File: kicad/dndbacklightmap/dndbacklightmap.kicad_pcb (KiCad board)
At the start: 2 copper layers, 76.2 x 76.2 mm, 40 parts, among them U1 SN65HVD230, U10 SLSS49E, U11 SLSS49E, U2 WeAct-STM32G431CoreBoard, U3 SLSS49E, U4 SLSS49E, U5 SLSS49E, U6 SLSS49E, U7 SLSS49E, U8 SLSS49E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

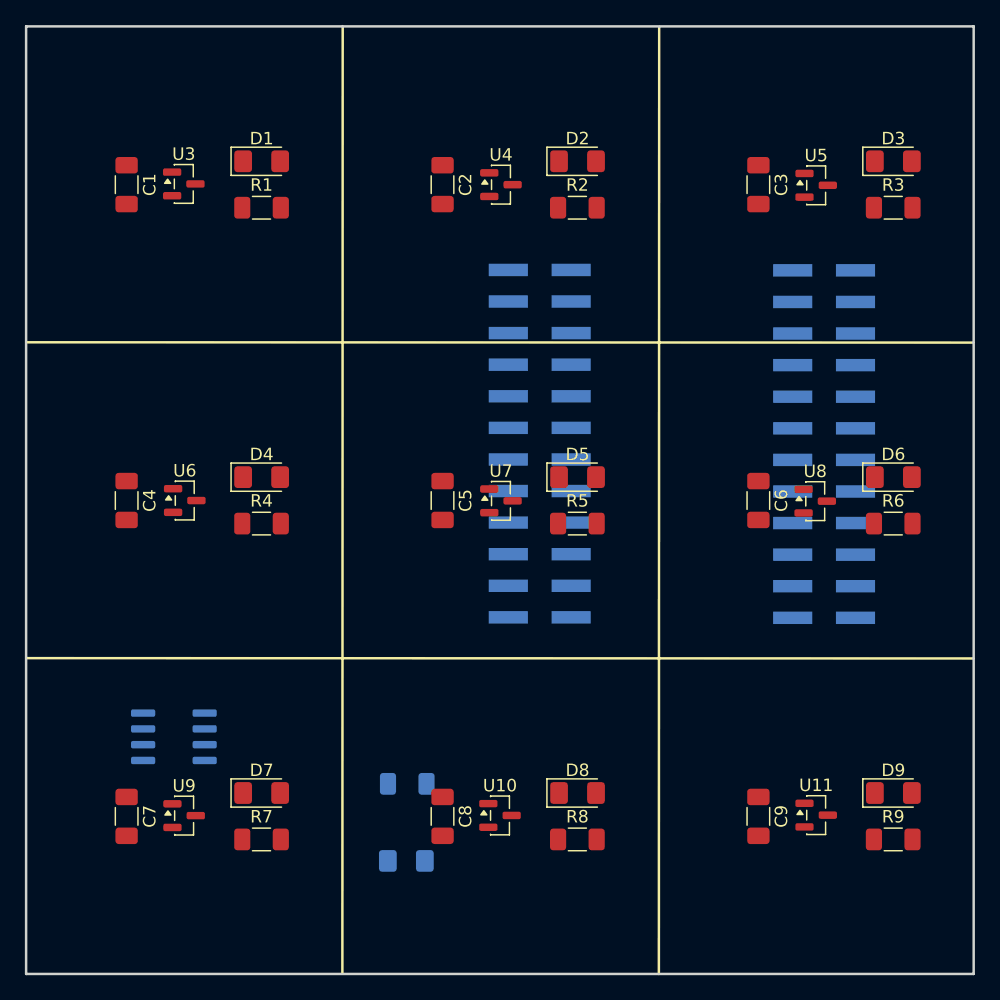
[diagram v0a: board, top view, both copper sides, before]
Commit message: rotation of components
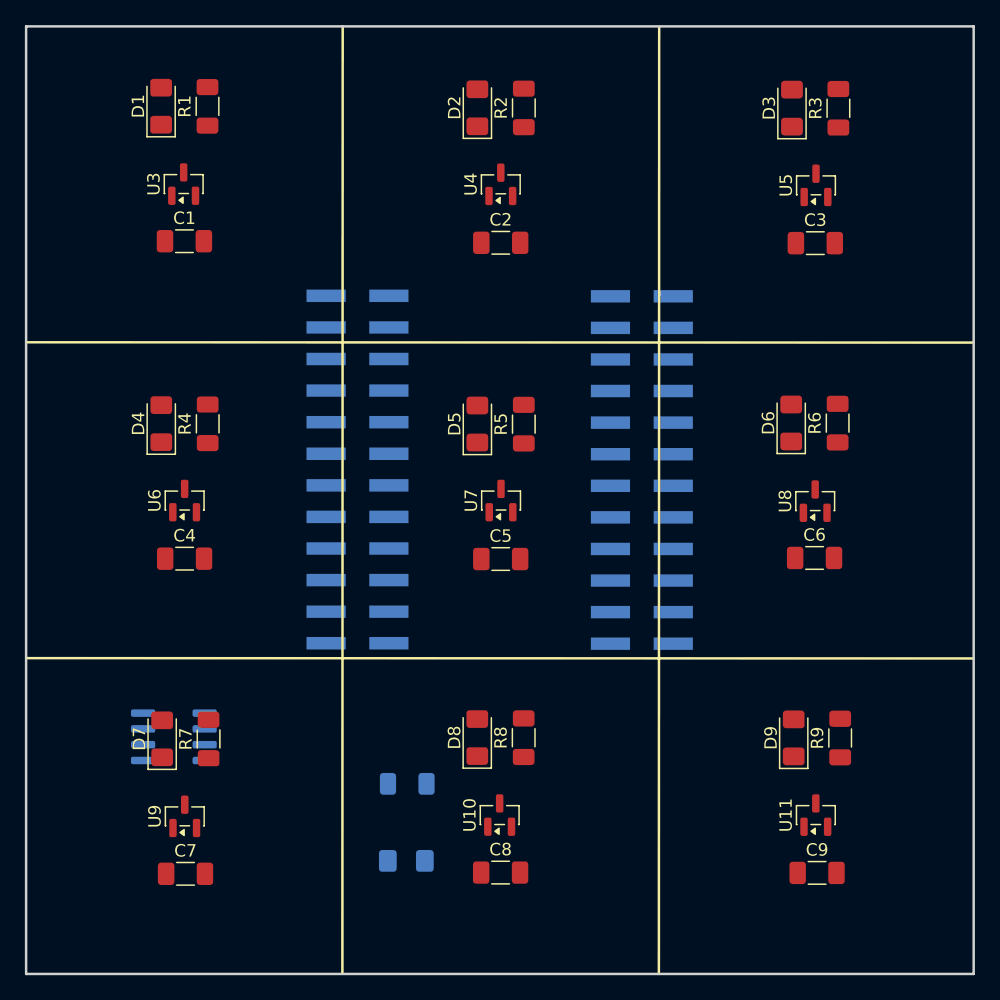
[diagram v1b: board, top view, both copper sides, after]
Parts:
- moved U2 14.8 mm to (146.0, 73.3)
- moved D6 9.30 mm to (155.3, 90.5), turned to 90 degrees
- moved R8 9.25 mm to (133.8, 115.8), turned to 90 degrees
- moved R1 9.24 mm to (108.4, 65.0), turned to 90 degrees
- moved R6 9.23 mm to (159.1, 90.5), turned to 90 degrees
- moved D1 9.22 mm to (104.6, 65.0), turned to 90 degrees
- moved D8 9.21 mm to (130.1, 115.8), turned to 90 degrees
- moved D3 9.21 mm to (155.4, 65.2), turned to 90 degrees
- moved R9 9.20 mm to (159.3, 115.8), turned to 90 degrees
- moved D9 9.16 mm to (155.5, 115.8), turned to 90 degrees
- moved D4 9.15 mm to (104.7, 90.5), turned to 90 degrees
- moved R7 9.13 mm to (108.5, 115.9), turned to 90 degrees
- moved R3 9.13 mm to (159.1, 65.2), turned to 90 degrees
- moved D2 9.13 mm to (130.1, 65.1), turned to 90 degrees
- moved R4 9.12 mm to (108.4, 90.6), turned to 90 degrees
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
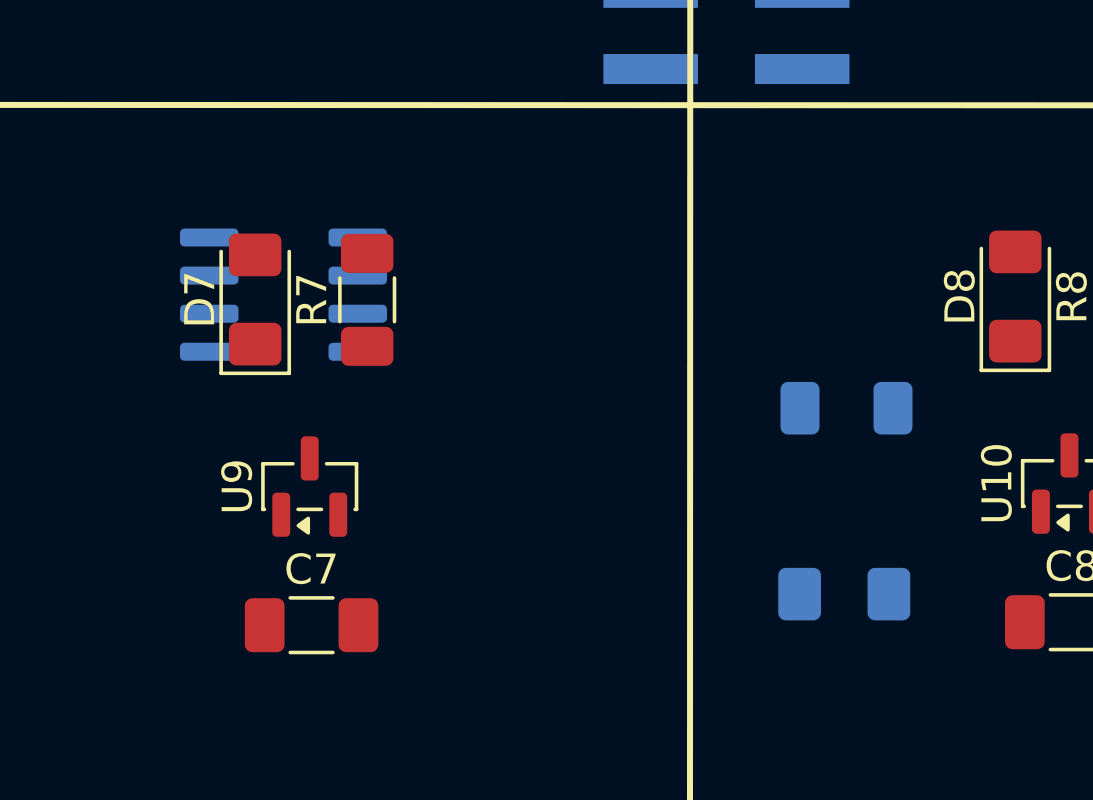
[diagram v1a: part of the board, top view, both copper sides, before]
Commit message: rotation of components
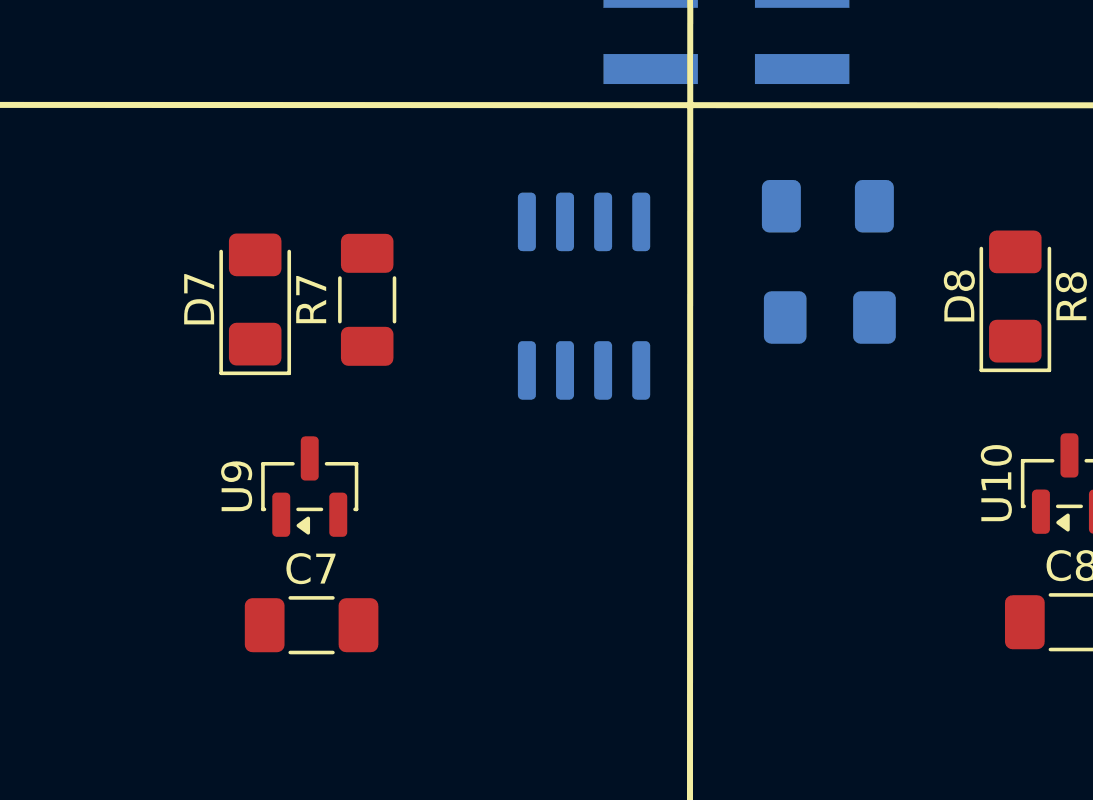
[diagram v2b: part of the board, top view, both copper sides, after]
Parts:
- moved U1 10.0 mm to (115.7, 115.8), turned to -90 degrees
- moved D10 9.23 mm to (123.9, 116.5)
- moved R10 6.76 mm to (123.8, 112.8)
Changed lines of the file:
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@@
 	(footprint "Resistor_SMD:R_1206_3216Metric_Pad1.30x1.75mm_HandSolder"
 		(layer "B.Cu")
-		(at 124.4451 119.507)
+		(at 123.8244 112.776)
 		(descr "Resistor SMD 1206 (3216 Metric), square (rectangular) end terminal, IPC-7351 nominal with elongated pad for handsoldering. (Body size source: IPC-SM-782 page 72, https://www.pcb-3d.com/wordpress/wp-content/uploads/ipc-sm-782a_amendment_1_and_2.pdf), generated with kicad-footprint-generator")
 		(tags "resistor handsolder")
@@
 	(footprint "Package_SO:SOIC-8_3.9x4.9mm_P1.27mm"
 		(layer "B.Cu")
-		(at 105.6782 115.7224)
+		(at 115.697 115.7732 -90)
 		(descr "SOIC, 8 Pin (JEDEC MS-012AA, https://www.analog.com/media/en/package-pcb-resources/package/pkg_pdf/soic_narrow-r/r_8.pdf), generated with kicad-footprint-generator ipc_gullwing_generator.py")
 		(tags "SOIC SO")
 		(property "Reference" "U1"
-			(at 0 3.4 180)
+			(at 0 3.4 90)
 			(layer "B.SilkS")
 			(effects
@@
 		)
 		(property "Value" "SN65HVD230"
-			(at 0 -3.4 180)
+			(at 0 -3.4 90)
 			(layer "B.Fab")
 			(effects
@@
 		)
 		(property "Datasheet" "http://www.ti.com/lit/ds/symlink/sn65hvd230.pdf"
-			(at 0 0 180)
+			(at 0 0 90)
 			(layer "B.Fab")
 			(hide yes)
@@
 		)
 		(property "Description" "CAN Bus Transceivers, 3.3V, 1Mbps, Low-Power capabilities, SOIC-8"
-			(at 0 0 180)
+			(at 0 0 90)
 			(layer "B.Fab")
 			(hide yes)
@@
 		(attr smd)
 		(fp_line
+			(start -2.06 2.56)
+			(end 2.06 2.56)
+			(stroke
+				(width 0.12)
+				(type solid)
+			)
+			(layer "B.SilkS")
+		)
+		(fp_line
+			(start 2.06 2.56)
+			(end 2.06 2.465)
+			(stroke
+				(width 0.12)
+				(type solid)
+			)
+			(layer "B.SilkS")
+		)
+		(fp_line
+			(start -2.06 2.465)
+			(end -2.06 2.56)
+			(stroke
+				(width 0.12)
+				(type solid)
+			)
+			(layer "B.SilkS")
+		)
+		(fp_line
+			(start 2.06 -2.465)
+			(end 2.06 -2.56)
+			(stroke
+				(width 0.12)
+				(type solid)
+			)
+			(layer "B.SilkS")
+		)
+		(fp_line
 			(start -2.06 -2.56)
 			(end -2.06 -2.465)
@@
 		)
 		(fp_line
-			(start -2.06 2.465)
-			(end -2.06 2.56)
-			(stroke
-				(width 0.12)
-				(type solid)
-			)
-			(layer "B.SilkS")
-		)
-		(fp_line
-			(start -2.06 2.56)
-			(end 2.06 2.56)
-			(stroke
-				(width 0.12)
-				(type solid)
-			)
-			(layer "B.SilkS")
-		)
-		(fp_line
 			(start 2.06 -2.56)
 			(end -2.06 -2.56)
-			(stroke
-				(width 0.12)
-				(type solid)
-			)
-			(layer "B.SilkS")
-		)
-		(fp_line
-			(start 2.06 -2.465)
-			(end 2.06 -2.56)
-			(stroke
-				(width 0.12)
-				(type solid)
-			)
-			(layer "B.SilkS")
-		)
-		(fp_line
-			(start 2.06 2.56)
-			(end 2.06 2.465)
 			(stroke
 				(width 0.12)
@@
 		)
 		(fp_line
+			(start -2.2 2.7)
+			(end 2.2 2.7)
+			(stroke
+				(width 0.05)
+				(type solid)
+			)
+			(layer "B.CrtYd")
+		)
+		(fp_line
+			(start 2.2 2.7)
+			(end 2.2 2.46)
+			(stroke
+				(width 0.05)
+				(type solid)
+			)
+			(layer "B.CrtYd")
+		)
+		(fp_line
+			(start -3.7 2.46)
+			(end -2.2 2.46)
+			(stroke
+				(width 0.05)
+				(type solid)
+			)
+			(layer "B.CrtYd")
+		)
+		(fp_line
+			(start -2.2 2.46)
+			(end -2.2 2.7)
+			(stroke
+				(width 0.05)
+				(type solid)
+			)
+			(layer "B.CrtYd")
+		)
+		(fp_line
+			(start 2.2 2.46)
+			(end 3.7 2.46)
+			(stroke
+				(width 0.05)
+				(type solid)
+			)
+			(layer "B.CrtYd")
+		)
+		(fp_line
+			(start 3.7 2.46)
+			(end 3.7 -2.46)
+			(stroke
+				(width 0.05)
+				(type solid)
+			)
+			(layer "B.CrtYd")
+		)
+		(fp_line
 			(start -3.7 -2.46)
 			(end -3.7 2.46)
@@
 		)
 		(fp_line
-			(start -3.7 2.46)
-			(end -2.2 2.46)
+			(start -2.2 -2.46)
+			(end -3.7 -2.46)
+			(stroke
+				(width 0.05)
+				(type solid)
+			)
+			(layer "B.CrtYd")
+		)
+		(fp_line
+			(start 2.2 -2.46)
+			(end 2.2 -2.7)
+			(stroke
+				(width 0.05)
+				(type solid)
+			)
+			(layer "B.CrtYd")
+		)
+		(fp_line
+			(start 3.7 -2.46)
+			(end 2.2 -2.46)
 			(stroke
 				(width 0.05)
@@
 		)
 		(fp_line
-			(start -2.2 -2.46)
-			(end -3.7 -2.46)
-			(stroke
-				(width 0.05)
-				(type solid)
-			)
-			(layer "B.CrtYd")
-		)
-		(fp_line
-			(start -2.2 2.46)
-			(end -2.2 2.7)
-			(stroke
-				(width 0.05)
-				(type solid)
-			)
-			(layer "B.CrtYd")
-		)
-		(fp_line
-			(start -2.2 2.7)
-			(end 2.2 2.7)
-			(stroke
-				(width 0.05)
-				(type solid)
-			)
-			(layer "B.CrtYd")
-		)
-		(fp_line
 			(start 2.2 -2.7)
 			(end -2.2 -2.7)
-			(stroke
-				(width 0.05)
-				(type solid)
-			)
-			(layer "B.CrtYd")
-		)
-		(fp_line
-			(start 2.2 -2.46)
-			(end 2.2 -2.7)
-			(stroke
-				(width 0.05)
-				(type solid)
-			)
-			(layer "B.CrtYd")
-		)
-		(fp_line
-			(start 2.2 2.46)
-			(end 3.7 2.46)
-			(stroke
-				(width 0.05)
-				(type solid)
-			)
-			(layer "B.CrtYd")
-		)
-		(fp_line
-			(start 2.2 2.7)
-			(end 2.2 2.46)
-			(stroke
-				(width 0.05)
-				(type solid)
-			)
-			(layer "B.CrtYd")
-		)
-		(fp_line
-			(start 3.7 -2.46)
-			(end 2.2 -2.46)
-			(stroke
-				(width 0.05)
-				(type solid)
-			)
-			(layer "B.CrtYd")
-		)
-		(fp_line
-			(start 3.7 2.46)
-			(end 3.7 -2.46)
 			(stroke
 				(width 0.05)
@@
 		)
 		(fp_text user "${REFERENCE}"
-			(at 0 0 90)
+			(at 0 0 0)
 			(layer "B.Fab")
 			(effects
@@
 		)
 		(pad "1" smd roundrect
-			(at -2.475 1.905)
+			(at -2.475 1.905 270)
 			(size 1.95 0.6)
 			(layers "B.Cu" "B.Mask" "B.Paste")
@@
 		)
 		(pad "2" smd roundrect
-			(at -2.475 0.635)
+			(at -2.475 0.635 270)
 			(size 1.95 0.6)
 			(layers "B.Cu" "B.Mask" "B.Paste")
@@
 		)
 		(pad "3" smd roundrect
-			(at -2.475 -0.635)
+			(at -2.475 -0.635 270)
 			(size 1.95 0.6)
 			(layers "B.Cu" "B.Mask" "B.Paste")
@@
 		)
 		(pad "4" smd roundrect
-			(at -2.475 -1.905)
+			(at -2.475 -1.905 270)
 			(size 1.95 0.6)
 			(layers "B.Cu" "B.Mask" "B.Paste")
@@
 		)
 		(pad "5" smd roundrect
-			(at 2.475 -1.905)
+			(at 2.475 -1.905 270)
 			(size 1.95 0.6)
 			(layers "B.Cu" "B.Mask" "B.Paste")
@@
 		)
 		(pad "6" smd roundrect
-			(at 2.475 -0.635)
+			(at 2.475 -0.635 270)
 			(size 1.95 0.6)
 			(layers "B.Cu" "B.Mask" "B.Paste")
@@
 		)
 		(pad "7" smd roundrect
-			(at 2.475 0.635)
+			(at 2.475 0.635 270)
 			(size 1.95 0.6)
 			(layers "B.Cu" "B.Mask" "B.Paste")
@@
 		)
 		(pad "8" smd roundrect
-			(at 2.475 1.905)
+			(at 2.475 1.905 270)
 			(size 1.95 0.6)
 			(layers "B.Cu" "B.Mask" "B.Paste")
@@
 	(footprint "LED_SMD:LED_1206_3216Metric_Pad1.42x1.75mm_HandSolder"
 		(layer "B.Cu")
-		(at 124.3695 125.7046)
+		(at 123.8901 116.4844)
 		(descr "LED SMD 1206 (3216 Metric), square (rectangular) end terminal, IPC-7351 nominal, (Body size source: http://www.tortai-tech.com/upload/download/2011102023233369053.pdf), generated with kicad-footprint-generator")
 		(tags "LED handsolder")
